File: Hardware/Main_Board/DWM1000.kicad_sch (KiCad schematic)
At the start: 0 parts

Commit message: Mixed in all of Layth's work, and added extra sheets
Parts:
- added U3: ~, symbol ESP32-Symbols:STM32N6
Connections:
- new net 5V: U3.1 (5V), U3.17 (5V), U3.19 (5V), U3.35 (5V)
- new net GND: U3.18 (GND), U3.2 (GND), U3.20 (GND), U3.36 (GND)
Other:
- note added: "- Delete all this and replace w/ whatever notes are relevant to the schematic once the schematic is done. - For power and UART, use the 5V0 and {UART} labels. - Take note of whichever UART you connect the ESP to (1, 2, 3, 4) - Add anything else you want, ie status LEDs, decoupling capacitor, etc. Arduino shield schematics are good examples - Any additional parts should be: - Available on JLCPCB, 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"
- note added: "Design Notes"
- note added: "Global/Hierarchcal Labels"

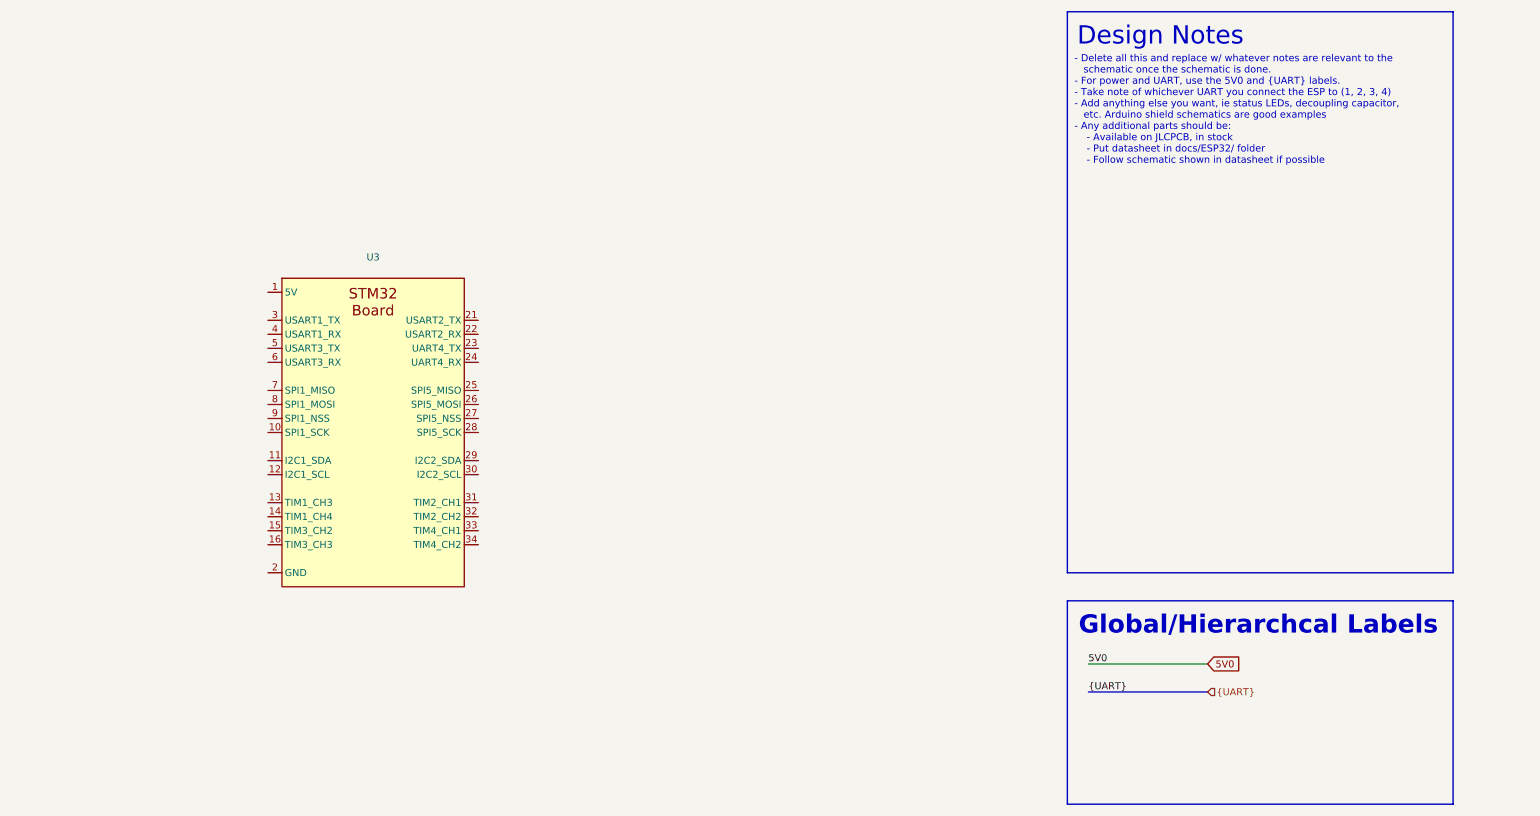
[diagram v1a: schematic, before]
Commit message: On behalf of Panuha and Layth: Added inital schematics for Main Board
- Added initial power units, 3v3 LDO remains
- Added buses for the ESP, UWB, and STM boards
- Connector sheet, footprint assignment, ERC check, etc remains.
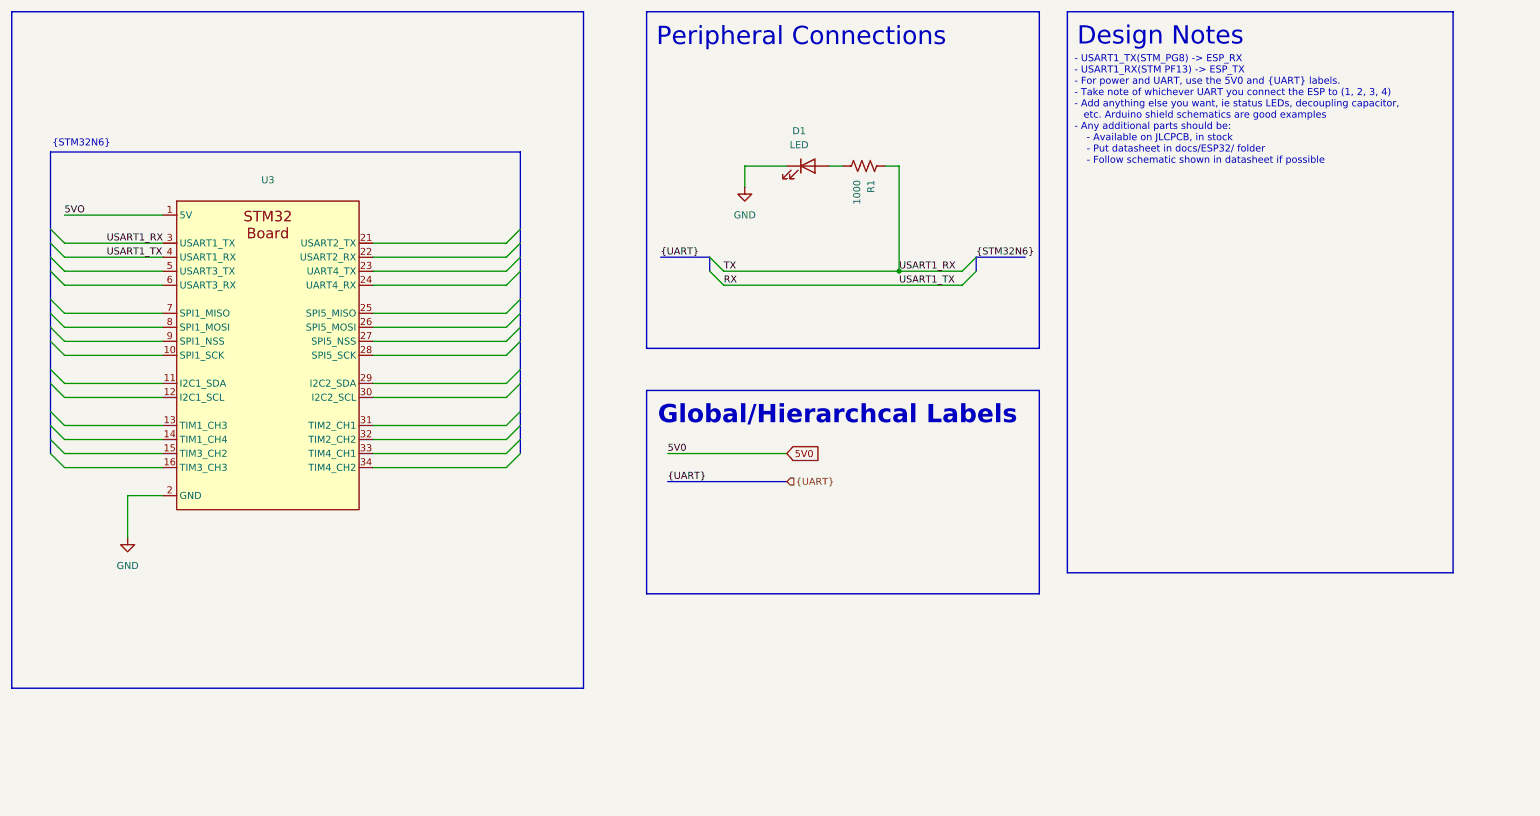
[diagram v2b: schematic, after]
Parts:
- added D1: LED, symbol Device:LED
- added R1: 1000, symbol Device:R_US
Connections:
- net GND: now also D1.1 (K)
- net TX: now reaches U3.3 (USART1_TX)
- net TX: now also R1.1
- net RX: now reaches U3.4 (USART1_RX)
- new net: D1.2 (A), R1.2
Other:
- note added: "- USART1_TX(STM_PG8) -> ESP_RX - USART1_RX(STM PF13) -> ESP_TX - For power and UART, use the 5V0 and {UART} labels. - Take note of whichever UART you connect the ESP to (1, 2, 3, 4) - Add anything else you want, ie status LEDs, decoupling capacitor, etc. Arduino shield schematics are good examples - Any additional parts should be: - Available on JLCPCB, in stock - Put datasheet in docs/ESP32/ fol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"
- note added: "Peripheral Connections"
- note added: "{STM32N6}"
- note removed: "- Delete all this and replace w/ whatever notes are relevant to the schematic once the schematic is done. - For power and UART, use the 5V0 and {UART} labels. - Take note of whichever UART you connect the ESP to (1, 2, 3, 4) - Add anything else you want, ie status LEDs, decoupling capacitor, etc. Arduino shield schematics are good examples - Any additional parts should be: - Available on JLCPCB, 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"
- moved on the sheet: U3

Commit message: Added all the main connectors
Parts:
- renumbered D1 to D2
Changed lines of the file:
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@@
 		(on_board yes)
 		(dnp no)
-		(property "Reference" "D1"
+		(property "Reference" "D2"
 			(at 162.2425 40.64 0)
 			(effects
@@
 			(project ""
 				(path "/3bfaeaa6-4337-4b5f-9f42-0e28df6ecb69/7b06a695-7782-48c9-8e2f-bf71bfa2a546"
-					(reference "D1")
+					(reference "D2")
 					(unit 1)
 				)
